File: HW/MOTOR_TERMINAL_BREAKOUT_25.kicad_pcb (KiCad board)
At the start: 2 copper layers, 25 x 33 mm, 12 parts

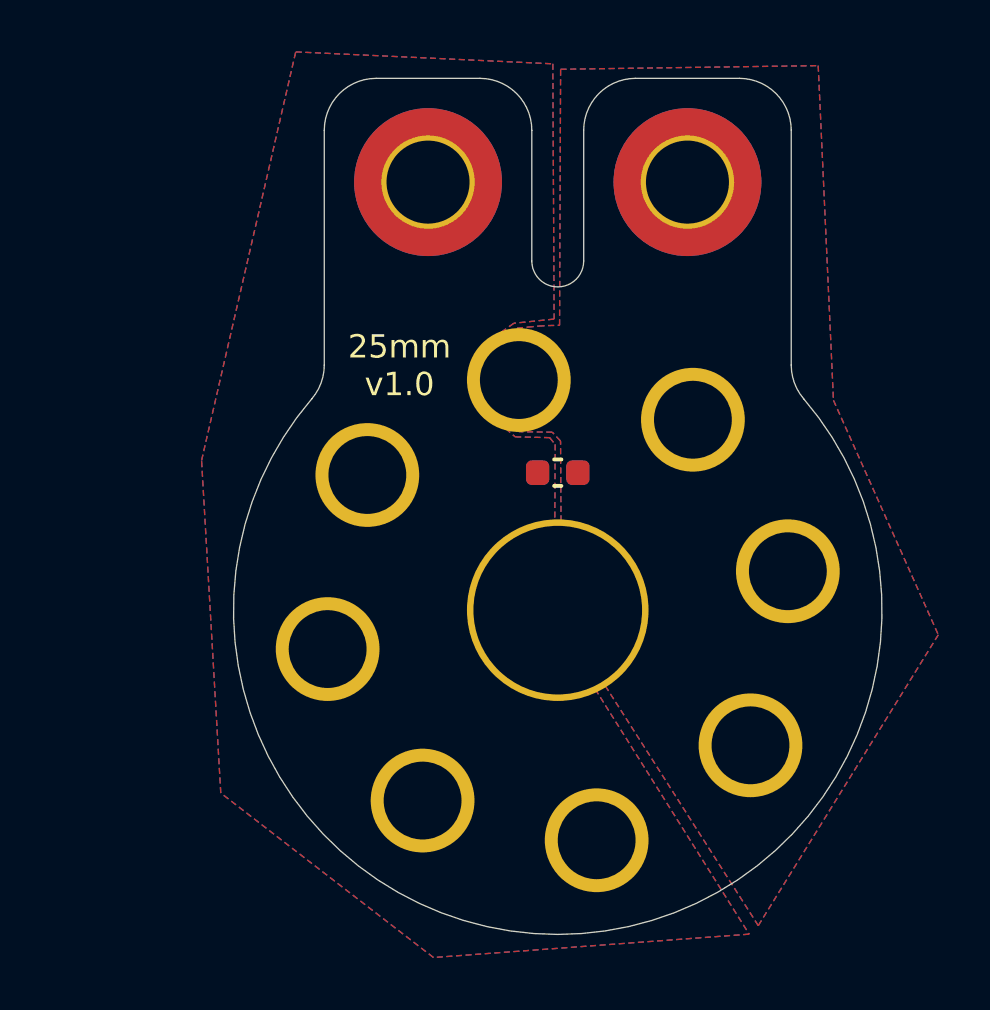
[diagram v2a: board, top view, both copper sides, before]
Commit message: Fix issue hole position issue.
Holes positions did not allow motor terminals to align with bolt holes
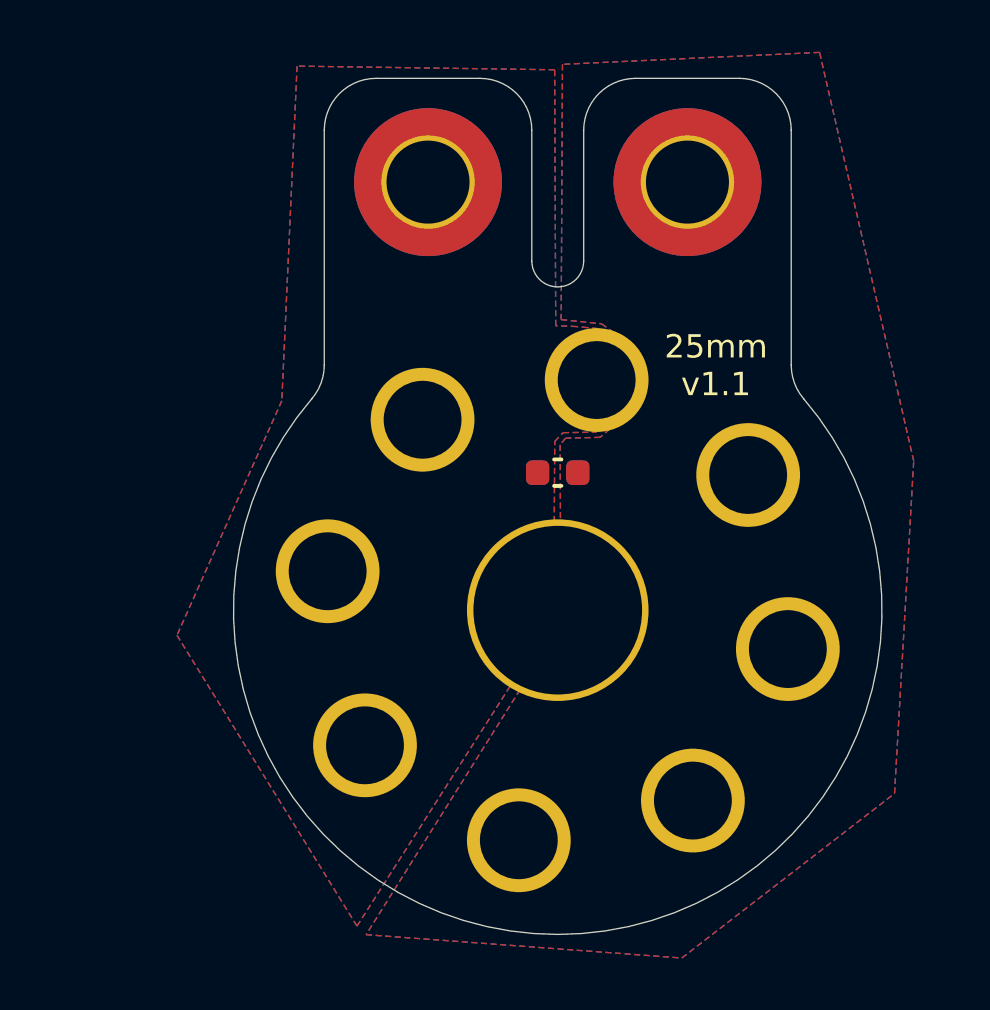
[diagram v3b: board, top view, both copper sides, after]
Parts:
- moved H4 17.7 mm to (228.9, 151.5)
- moved H9 17.7 mm to (211.1, 148.5)
- moved H3 14.9 mm to (212.6, 155.2)
- moved H10 14.7 mm to (227.3, 144.8)
- moved H6 10.4 mm to (225.2, 157.3)
- moved H7 10.4 mm to (214.8, 142.7)
- moved H5 3.00 mm to (221.5, 141.1)
- moved H8 3.00 mm to (218.5, 158.9)
- turned C1 to 0 degrees
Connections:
- H1 pad 1: +BATT -> GND
- H2 pad 1: GND -> +BATT
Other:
- board text added: "25mm v1.1"
- board text removed: "25mm v1.0"
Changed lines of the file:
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@@
   (net 2 "+BATT")
   (footprint "MountingHole:MountingHole_3mm_Pad_TopBottom" (layer "F.Cu")
-    (at 225.21 142.66)
-    (descr "Mounting Hole 3mm")
-    (tags "mounting hole 3mm")
-    (property "Sheetfile" "MOTOR_TERMINAL_BREAKOUT_22.kicad_sch")
+    (at 214.79 142.66)
+    (descr "Mounting Hole 3mm")
+    (tags "mounting hole 3mm")
+    (property "Sheetfile" "MOTOR_TERMINAL_BREAKOUT_25.kicad_sch")
     (property "Sheetname" "")
     (attr exclude_from_pos_files)
@@
   )
   (footprint "MountingHole:MountingHole_3mm_Pad_TopBottom" (layer "F.Cu")
-    (at 221.5 158.87)
-    (descr "Mounting Hole 3mm")
-    (tags "mounting hole 3mm")
-    (property "Sheetfile" "MOTOR_TERMINAL_BREAKOUT_22.kicad_sch")
+    (at 218.5 158.87)
+    (descr "Mounting Hole 3mm")
+    (tags "mounting hole 3mm")
+    (property "Sheetfile" "MOTOR_TERMINAL_BREAKOUT_25.kicad_sch")
     (property "Sheetname" "")
     (attr exclude_from_pos_files)
@@
   )
   (footprint "MountingHole:MountingHole_3mm_Pad_TopBottom" (layer "F.Cu")
-    (at 218.5 141.13)
-    (descr "Mounting Hole 3mm")
-    (tags "mounting hole 3mm")
-    (property "Sheetfile" "MOTOR_TERMINAL_BREAKOUT_22.kicad_sch")
+    (at 221.5 141.13)
+    (descr "Mounting Hole 3mm")
+    (tags "mounting hole 3mm")
+    (property "Sheetfile" "MOTOR_TERMINAL_BREAKOUT_25.kicad_sch")
     (property "Sheetname" "")
     (attr exclude_from_pos_files)
@@
   )
   (footprint "MountingHole:MountingHole_3mm_Pad_TopBottom" (layer "F.Cu")
-    (at 211.13 151.5)
-    (descr "Mounting Hole 3mm")
-    (tags "mounting hole 3mm")
-    (property "Sheetfile" "MOTOR_TERMINAL_BREAKOUT_22.kicad_sch")
+    (at 228.87 151.5)
+    (descr "Mounting Hole 3mm")
+    (tags "mounting hole 3mm")
+    (property "Sheetfile" "MOTOR_TERMINAL_BREAKOUT_25.kicad_sch")
     (property "Sheetname" "")
     (attr exclude_from_pos_files)
@@
     (descr "Mounting Hole 3.2mm, M3, ISO7380")
     (tags "mounting hole 3.2mm m3 iso7380")
-    (property "Sheetfile" "MOTOR_TERMINAL_BREAKOUT_22.kicad_sch")
+    (property "Sheetfile" "MOTOR_TERMINAL_BREAKOUT_25.kicad_sch")
     (property "Sheetname" "")
     (attr exclude_from_pos_files)
@@
     (fp_circle (center 0 0) (end 3.1 0) (layer "F.CrtYd") (width 0.05) (fill none))
     (pad "1" thru_hole circle locked (at 0 0) (size 3.6 3.6) (drill 3.2) (layers *.Cu *.Mask)
-      (net 2 "+BATT") (pinfunction "1") (pintype "input"))
+      (net 1 "GND") (pinfunction "1") (pintype "input"))
     (pad "1" connect circle locked (at 0 0) (size 5.7 5.7) (layers "F.Cu" "F.Mask")
-      (net 2 "+BATT") (pinfunction "1") (pintype "input"))
+      (net 1 "GND") (pinfunction "1") (pintype "input"))
     (pad "1" connect circle locked (at 0 0) (size 5.7 5.7) (layers "B.Cu" "B.Mask")
-      (net 2 "+BATT") (pinfunction "1") (pintype "input"))
+      (net 1 "GND") (pinfunction "1") (pintype "input"))
   )
   (footprint "MountingHole:MountingHole_6.5mm" (layer "F.Cu")
@@
   )
   (footprint "MountingHole:MountingHole_3mm_Pad_TopBottom" (layer "F.Cu")
-    (at 228.87 148.5)
-    (descr "Mounting Hole 3mm")
-    (tags "mounting hole 3mm")
-    (property "Sheetfile" "MOTOR_TERMINAL_BREAKOUT_22.kicad_sch")
+    (at 211.13 148.5)
+    (descr "Mounting Hole 3mm")
+    (tags "mounting hole 3mm")
+    (property "Sheetfile" "MOTOR_TERMINAL_BREAKOUT_25.kicad_sch")
     (property "Sheetname" "")
     (attr exclude_from_pos_files)
@@
   )
   (footprint "MountingHole:MountingHole_3mm_Pad_TopBottom" (layer "F.Cu")
-    (at 227.43 155.21)
-    (descr "Mounting Hole 3mm")
-    (tags "mounting hole 3mm")
-    (property "Sheetfile" "MOTOR_TERMINAL_BREAKOUT_22.kicad_sch")
+    (at 212.57 155.21)
+    (descr "Mounting Hole 3mm")
+    (tags "mounting hole 3mm")
+    (property "Sheetfile" "MOTOR_TERMINAL_BREAKOUT_25.kicad_sch")
     (property "Sheetname" "")
     (attr exclude_from_pos_files)
@@
     (descr "Mounting Hole 3.2mm, M3, ISO7380")
     (tags "mounting hole 3.2mm m3 iso7380")
-    (property "Sheetfile" "MOTOR_TERMINAL_BREAKOUT_22.kicad_sch")
+    (property "Sheetfile" "MOTOR_TERMINAL_BREAKOUT_25.kicad_sch")
     (property "Sheetname" "")
     (attr exclude_from_pos_files)
@@
     (fp_circle (center 0 0) (end 3.1 0) (layer "F.CrtYd") (width 0.05) (fill none))
     (pad "1" thru_hole circle locked (at 0 0) (size 3.6 3.6) (drill 3.2) (layers *.Cu *.Mask)
-      (net 1 "GND") (pinfunction "1") (pintype "input"))
+      (net 2 "+BATT") (pinfunction "1") (pintype "input"))
     (pad "1" connect circle locked (at 0 0) (size 5.7 5.7) (layers "B.Cu" "B.Mask")
-      (net 1 "GND") (pinfunction "1") (pintype "input"))
+      (net 2 "+BATT") (pinfunction "1") (pintype "input"))
     (pad "1" connect circle locked (at 0 0) (size 5.7 5.7) (layers "F.Cu" "F.Mask")
-      (net 1 "GND") (pinfunction "1") (pintype "input"))
+      (net 2 "+BATT") (pinfunction "1") (pintype "input"))
   )
   (footprint "C_Capacitor:C_0603" (layer "F.Cu")
-    (at 220 144.7 180)
-    (property "Sheetfile" "MOTOR_TERMINAL_BREAKOUT_22.kicad_sch")
+    (at 220 144.7)
+    (property "Sheetfile" "MOTOR_TERMINAL_BREAKOUT_25.kicad_sch")
     (property "Sheetname" "")
     (property "Size" "C_0603")
@@
     (fp_line (start -0.8 0.4) (end -0.8 -0.4) (layer "F.Fab") (width 0.1))
     (fp_line (start 0.8 0.4) (end -0.8 0.4) (layer "F.Fab") (width 0.1))
-    (pad "1" smd roundrect (at -0.775 0 180) (size 0.9 0.95) (layers "F.Cu" "F.Paste" "F.Mask") (roundrect_rratio 0.25)
+    (pad "1" smd roundrect (at -0.775 0) (size 0.9 0.95) (layers "F.Cu" "F.Paste" "F.Mask") (roundrect_rratio 0.25)
       (net 2 "+BATT") (pintype "passive"))
-    (pad "2" smd roundrect (at 0.775 0 180) (size 0.9 0.95) (layers "F.Cu" "F.Paste" "F.Mask") (roundrect_rratio 0.25)
+    (pad "2" smd roundrect (at 0.775 0) (size 0.9 0.95) (layers "F.Cu" "F.Paste" "F.Mask") (roundrect_rratio 0.25)
       (net 1 "GND") (pintype "passive"))
     (model "${LAMBO_LIB}/Step/cap/CAP0603.step"
@@
   )
   (footprint "MountingHole:MountingHole_3mm_Pad_TopBottom" (layer "F.Cu")
-    (at 212.66 144.79)
-    (descr "Mounting Hole 3mm")
-    (tags "mounting hole 3mm")
-    (property "Sheetfile" "MOTOR_TERMINAL_BREAKOUT_22.kicad_sch")
+    (at 227.34 144.79)
+    (descr "Mounting Hole 3mm")
+    (tags "mounting hole 3mm")
+    (property "Sheetfile" "MOTOR_TERMINAL_BREAKOUT_25.kicad_sch")
     (property "Sheetname" "")
     (attr exclude_from_pos_files)
@@
   )
   (footprint "MountingHole:MountingHole_3mm_Pad_TopBottom" (layer "F.Cu")
-    (at 214.79 157.34)
-    (descr "Mounting Hole 3mm")
-    (tags "mounting hole 3mm")
-    (property "Sheetfile" "MOTOR_TERMINAL_BREAKOUT_22.kicad_sch")
+    (at 225.21 157.34)
+    (descr "Mounting Hole 3mm")
+    (tags "mounting hole 3mm")
+    (property "Sheetfile" "MOTOR_TERMINAL_BREAKOUT_25.kicad_sch")
     (property "Sheetname" "")
     (attr exclude_from_pos_files)
@@
   )
   (gr_rect (start 213.25 131.69) (end 216.77 135.85) (layer "F.Mask") (width 3.5) (fill none))
-  (gr_arc (start 218.5 141.14) (mid 227.623587 145.234196) (end 227.33 155.23) (layer "F.Mask") (width 4))
+  (gr_arc (start 227.34 144.79) (mid 227.61198 154.775817) (end 218.5 158.87) (layer "F.Mask") (width 4))
   (gr_rect (start 223.25 131.73) (end 226.77 135.89) (layer "F.Mask") (width 3.5) (fill none))
-  (gr_arc (start 221.49 158.88) (mid 212.391236 154.778632) (end 212.58 144.8) (layer "F.Mask") (width 4))
+  (gr_arc (start 212.57 155.21) (mid 212.403398 145.232486) (end 221.5 141.13) (layer "F.Mask") (width 4))
   (gr_arc (start 217 129.5) (mid 218.414214 130.085786) (end 219 131.5) (layer "Edge.Cuts") (width 0.05))
   (gr_line (start 221 136.540064) (end 221 131.5) (layer "Edge.Cuts") (width 0.05))
@@
   (gr_line (start 219 131.5) (end 219 136.540064) (layer "Edge.Cuts") (width 0.05))
   (gr_arc (start 221 136.540064) (mid 220 137.540064) (end 219 136.540064) (layer "Edge.Cuts") (width 0.05))
-  (gr_text "25mm\nv1.0" (at 213.9 140.57) (layer "F.SilkS")
+  (gr_text "25mm\nv1.1" (at 226.1 140.57) (layer "F.SilkS")
     (effects (font (size 0.9 0.9) (thickness 0.2)))
   )
@@
     (polygon
       (pts
-        (xy 230.628218 141.910808)
-        (xy 234.67 150.95)
-        (xy 227.73 162.16)
-        (xy 220.148218 150.280808)
-        (xy 220.108218 143.480808)
-        (xy 219.79 143.14)
-        (xy 218.5 143.12)
-        (xy 218.43 139.13)
-        (xy 218.84 139.09)
-        (xy 219.26 139.05)
-        (xy 219.63 139.03)
-        (xy 220.07 139.02)
-        (xy 220.11 129.15)
-        (xy 230.04 129.01)
+        (xy 209.363564 141.93)
+        (xy 205.321782 150.969192)
+        (xy 212.261782 162.179192)
+        (xy 219.843564 150.3)
+        (xy 219.883564 143.5)
+        (xy 220.201782 143.159192)
+        (xy 221.491782 143.139192)
+        (xy 221.561782 139.149192)
+        (xy 221.151782 139.109192)
+        (xy 220.731782 139.069192)
+        (xy 220.361782 139.049192)
+        (xy 219.921782 139.039192)
+        (xy 219.881782 129.169192)
+        (xy 209.951782 129.029192)
       )
     )
@@
     (polygon
       (pts
-        (xy 219.81 128.94)
-        (xy 219.86 138.78)
-        (xy 218.31 138.94)
-        (xy 217.23 139.7)
-        (xy 216.74 140.69)
-        (xy 216.87 142.03)
-        (xy 218.36 143.32)
-        (xy 219.69 143.35)
-        (xy 219.9 143.61)
-        (xy 219.87 150.54)
-        (xy 227.38 162.49)
-        (xy 215.21 163.39)
-        (xy 207.01 157.05)
-        (xy 206.27 144.23)
-        (xy 209.9 128.48)
+        (xy 220.181782 128.959192)
+        (xy 220.131782 138.799192)
+        (xy 221.681782 138.959192)
+        (xy 222.761782 139.719192)
+        (xy 223.251782 140.709192)
+        (xy 223.121782 142.049192)
+        (xy 221.631782 143.339192)
+        (xy 220.301782 143.369192)
+        (xy 220.091782 143.629192)
+        (xy 220.121782 150.559192)
+        (xy 212.611782 162.509192)
+        (xy 224.781782 163.409192)
+        (xy 232.981782 157.069192)
+        (xy 233.721782 144.249192)
+        (xy 230.091782 128.499192)
       )
     )
